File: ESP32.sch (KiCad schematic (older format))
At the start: 28 parts, among them J201 Conn_02x13_Odd_Even, J202 Conn_02x10_Odd_Even, J203 Conn_01x02, U201 ESP32-WROOM-32D

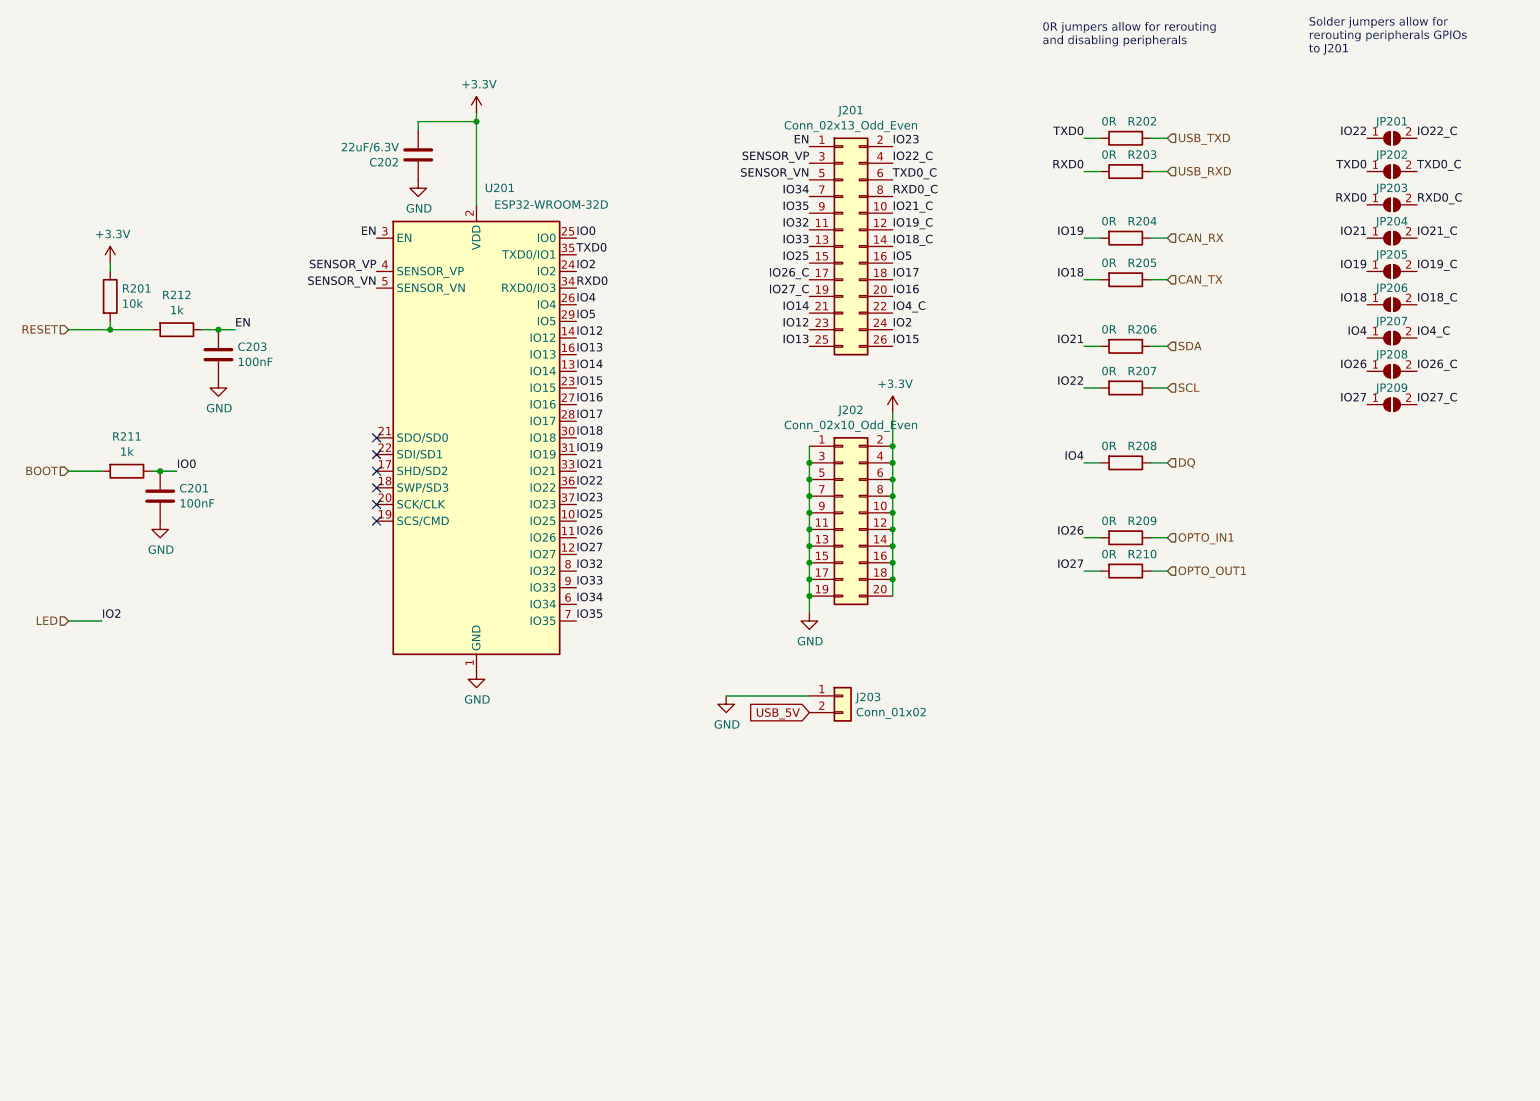
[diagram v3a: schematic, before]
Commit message: Change optocoupler types, improve ground planes and a lot of other smaller fixes
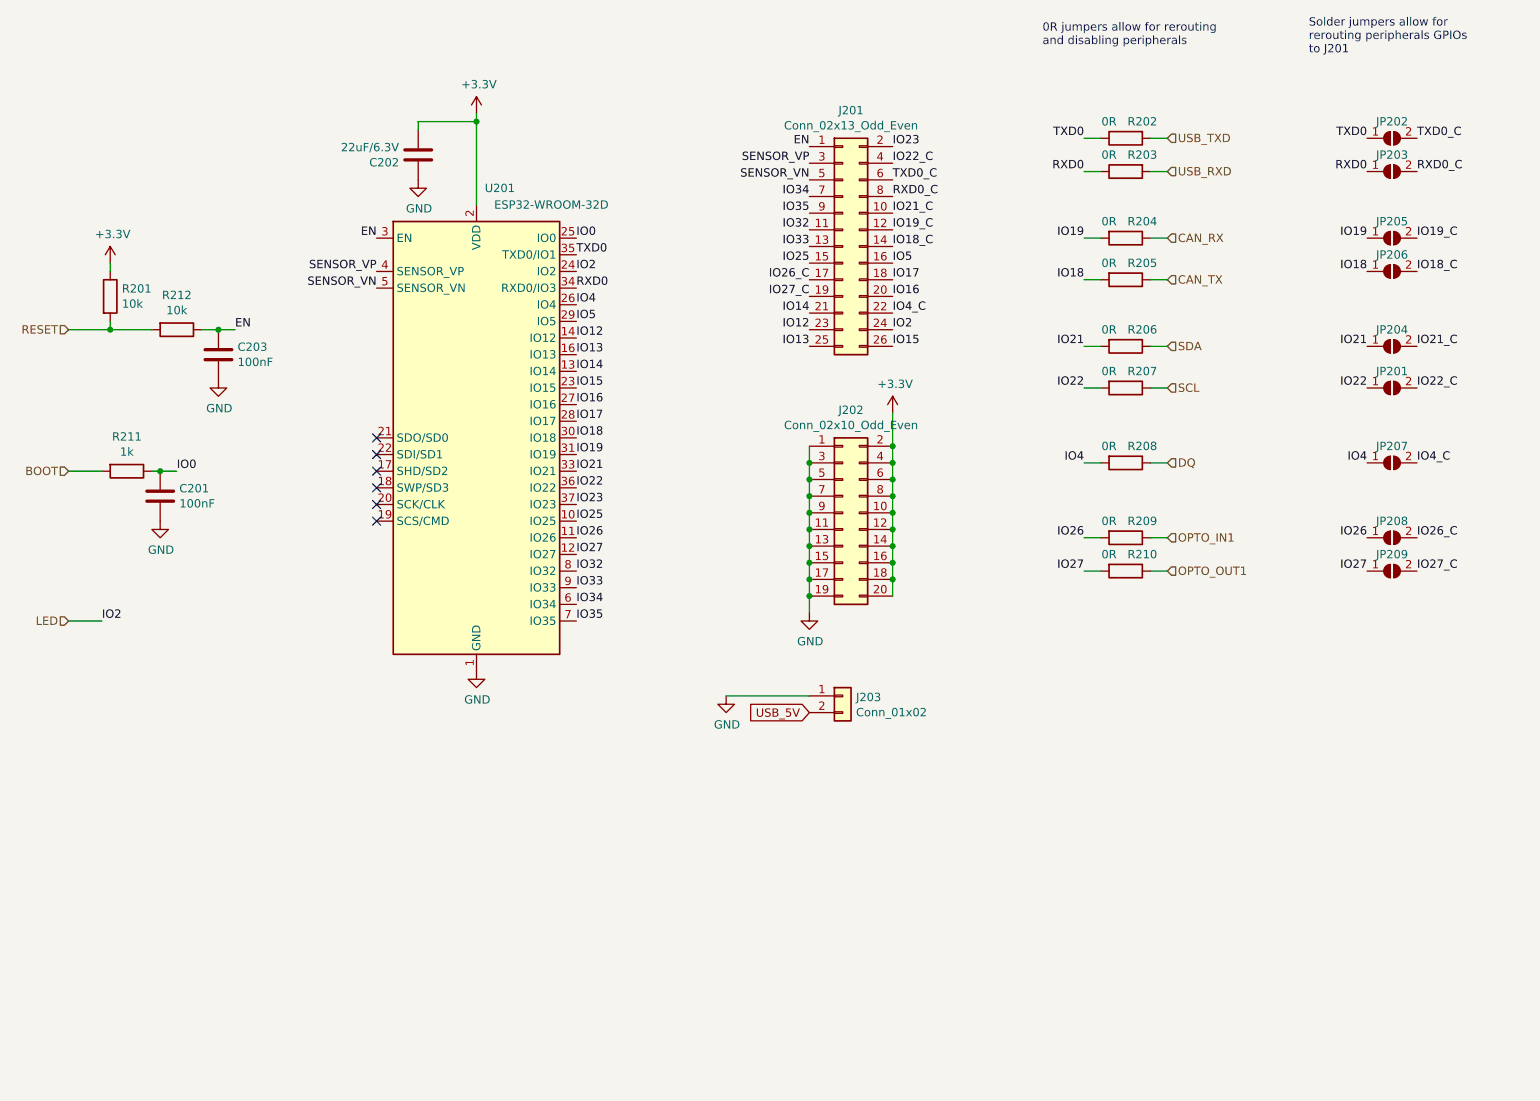
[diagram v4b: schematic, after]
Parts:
- R212: value 1k -> 10k; LCSC C11702 -> C25744
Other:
- moved on the sheet: JP201, JP202, JP203, JP204, JP205, JP206, JP207, JP208, JP209
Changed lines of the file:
@@
 P 1900 2600
 F 0 "R212" V 1693 2600 50  0000 C CNN
-F 1 "1k" V 1784 2600 50  0000 C CNN
+F 1 "10k" V 1784 2600 50  0000 C CNN
 F 2 "Resistor_SMD:R_0402_1005Metric" V 1830 2600 50  0001 C CNN
 F 3 "~" H 1900 2600 50  0001 C CNN
-F 4 "C11702" H 1900 2600 50  0001 C CNN "LCSC"
+F 4 "C25744" H 1900 2600 50  0001 C CNN "LCSC"
 	1    1900 2600
 	0    1    1    0
@@
 	1    0    0    -1
 $EndComp
+Text Label 9350 2950 0    50   ~ 0
+IO22_C
 Text Label 9350 1450 0    50   ~ 0
-IO22_C
+TXD0_C
 Text Label 9350 1650 0    50   ~ 0
-TXD0_C
-Text Label 9350 1850 0    50   ~ 0
 RXD0_C
+Text Label 9350 2700 0    50   ~ 0
+IO21_C
 Text Label 9350 2050 0    50   ~ 0
-IO21_C
+IO19_C
 Text Label 9350 2250 0    50   ~ 0
-IO19_C
-Text Label 9350 2450 0    50   ~ 0
 IO18_C
-Text Label 9350 2650 0    50   ~ 0
+Text Label 9350 3400 0    50   ~ 0
 IO4_C
-Text Label 9350 2850 0    50   ~ 0
+Text Label 9350 3850 0    50   ~ 0
 IO26_C
-Text Label 9350 3050 0    50   ~ 0
+Text Label 9350 4050 0    50   ~ 0
 IO27_C
+Text Label 9050 2950 2    50   ~ 0
+IO22
 Text Label 9050 1450 2    50   ~ 0
-IO22
+TXD0
 Text Label 9050 1650 2    50   ~ 0
-TXD0
-Text Label 9050 1850 2    50   ~ 0
 RXD0
+Text Label 9050 2700 2    50   ~ 0
+IO21
 Text Label 9050 2050 2    50   ~ 0
-IO21
+IO19
 Text Label 9050 2250 2    50   ~ 0
-IO19
-Text Label 9050 2450 2    50   ~ 0
 IO18
-Text Label 9050 2650 2    50   ~ 0
+Text Label 9050 3400 2    50   ~ 0
 IO4
-Text Label 9050 2850 2    50   ~ 0
+Text Label 9050 3850 2    50   ~ 0
 IO26
-Text Label 9050 3050 2    50   ~ 0
+Text Label 9050 4050 2    50   ~ 0
 IO27
 $Comp
 L Jumper:SolderJumper_2_Open JP201
 U 1 1 5FB7A6EE
+P 9200 2950
+F 0 "JP201" H 9200 3050 50  0000 C CNN
+F 1 "SolderJumper_2_Open" H 9200 3064 50  0001 C CNN
+F 2 "SH-ESP32:SolderJumper-2_P1.3mm_Open_TrianglePad_Narrow" H 9200 2950 50  0001 C CNN
+F 3 "~" H 9200 2950 50  0001 C CNN
+	1    9200 2950
+	1    0    0    -1
+$EndComp
+$Comp
+L Jumper:SolderJumper_2_Open JP202
+U 1 1 5FB7C918
 P 9200 1450
-F 0 "JP201" H 9200 1550 50  0000 C CNN
+F 0 "JP202" H 9200 1550 50  0000 C CNN
 F 1 "SolderJumper_2_Open" H 9200 1564 50  0001 C CNN
 F 2 "SH-ESP32:SolderJumper-2_P1.3mm_Open_TrianglePad_Narrow" H 9200 1450 50  0001 C CNN
@@
 $EndComp
 $Comp
-L Jumper:SolderJumper_2_Open JP202
-U 1 1 5FB7C918
+L Jumper:SolderJumper_2_Open JP203
+U 1 1 5FB7CDD7
 P 9200 1650
-F 0 "JP202" H 9200 1750 50  0000 C CNN
+F 0 "JP203" H 9200 1750 50  0000 C CNN
 F 1 "SolderJumper_2_Open" H 9200 1764 50  0001 C CNN
 F 2 "SH-ESP32:SolderJumper-2_P1.3mm_Open_TrianglePad_Narrow" H 9200 1650 50  0001 C CNN
@@
 $EndComp
 $Comp
-L Jumper:SolderJumper_2_Open JP203
-U 1 1 5FB7CDD7
-P 9200 1850
-F 0 "JP203" H 9200 1950 50  0000 C CNN
-F 1 "SolderJumper_2_Open" H 9200 1964 50  0001 C CNN
-F 2 "SH-ESP32:SolderJumper-2_P1.3mm_Open_TrianglePad_Narrow" H 9200 1850 50  0001 C CNN
-F 3 "~" H 9200 1850 50  0001 C CNN
-	1    9200 1850
-	1    0    0    -1
-$EndComp
-$Comp
 L Jumper:SolderJumper_2_Open JP204
 U 1 1 5FB7D1DC
+P 9200 2700
+F 0 "JP204" H 9200 2800 50  0000 C CNN
+F 1 "SolderJumper_2_Open" H 9200 2814 50  0001 C CNN
+F 2 "SH-ESP32:SolderJumper-2_P1.3mm_Open_TrianglePad_Narrow" H 9200 2700 50  0001 C CNN
+F 3 "~" H 9200 2700 50  0001 C CNN
+	1    9200 2700
+	1    0    0    -1
+$EndComp
+$Comp
+L Jumper:SolderJumper_2_Open JP205
+U 1 1 5FB7D48C
 P 9200 2050
-F 0 "JP204" H 9200 2150 50  0000 C CNN
+F 0 "JP205" H 9200 2150 50  0000 C CNN
 F 1 "SolderJumper_2_Open" H 9200 2164 50  0001 C CNN
 F 2 "SH-ESP32:SolderJumper-2_P1.3mm_Open_TrianglePad_Narrow" H 9200 2050 50  0001 C CNN
@@
 $EndComp
 $Comp
-L Jumper:SolderJumper_2_Open JP205
-U 1 1 5FB7D48C
+L Jumper:SolderJumper_2_Open JP206
+U 1 1 5FB7D7F6
 P 9200 2250
-F 0 "JP205" H 9200 2350 50  0000 C CNN
+F 0 "JP206" H 9200 2350 50  0000 C CNN
 F 1 "SolderJumper_2_Open" H 9200 2364 50  0001 C CNN
 F 2 "SH-ESP32:SolderJumper-2_P1.3mm_Open_TrianglePad_Narrow" H 9200 2250 50  0001 C CNN
@@
 $EndComp
 $Comp
-L Jumper:SolderJumper_2_Open JP206
-U 1 1 5FB7D7F6
-P 9200 2450
-F 0 "JP206" H 9200 2550 50  0000 C CNN
-F 1 "SolderJumper_2_Open" H 9200 2564 50  0001 C CNN
-F 2 "SH-ESP32:SolderJumper-2_P1.3mm_Open_TrianglePad_Narrow" H 9200 2450 50  0001 C CNN
-F 3 "~" H 9200 2450 50  0001 C CNN
-	1    9200 2450
-	1    0    0    -1
-$EndComp
-$Comp
 L Jumper:SolderJumper_2_Open JP207
 U 1 1 5FB7DA87
-P 9200 2650
-F 0 "JP207" H 9200 2750 50  0000 C CNN
-F 1 "SolderJumper_2_Open" H 9200 2764 50  0001 C CNN
-F 2 "SH-ESP32:SolderJumper-2_P1.3mm_Open_TrianglePad_Narrow" H 9200 2650 50  0001 C CNN
-F 3 "~" H 9200 2650 50  0001 C CNN
-	1    9200 2650
+P 9200 3400
+F 0 "JP207" H 9200 3500 50  0000 C CNN
+F 1 "SolderJumper_2_Open" H 9200 3514 50  0001 C CNN
+F 2 "SH-ESP32:SolderJumper-2_P1.3mm_Open_TrianglePad_Narrow" H 9200 3400 50  0001 C CNN
+F 3 "~" H 9200 3400 50  0001 C CNN
+	1    9200 3400
 	1    0    0    -1
 $EndComp
@@
 L Jumper:SolderJumper_2_Open JP208
 U 1 1 5FB7E3FF
-P 9200 2850
-F 0 "JP208" H 9200 2950 50  0000 C CNN
-F 1 "SolderJumper_2_Open" H 9200 2964 50  0001 C CNN
-F 2 "SH-ESP32:SolderJumper-2_P1.3mm_Open_TrianglePad_Narrow" H 9200 2850 50  0001 C CNN
-F 3 "~" H 9200 2850 50  0001 C CNN
-	1    9200 2850
+P 9200 3850
+F 0 "JP208" H 9200 3950 50  0000 C CNN
+F 1 "SolderJumper_2_Open" H 9200 3964 50  0001 C CNN
+F 2 "SH-ESP32:SolderJumper-2_P1.3mm_Open_TrianglePad_Narrow" H 9200 3850 50  0001 C CNN
+F 3 "~" H 9200 3850 50  0001 C CNN
+	1    9200 3850
 	1    0    0    -1
 $EndComp
@@
 L Jumper:SolderJumper_2_Open JP209
 U 1 1 5FB7EB87
-P 9200 3050
-F 0 "JP209" H 9200 3150 50  0000 C CNN
-F 1 "SolderJumper_2_Open" H 9200 3164 50  0001 C CNN
-F 2 "SH-ESP32:SolderJumper-2_P1.3mm_Open_TrianglePad_Narrow" H 9200 3050 50  0001 C CNN
-F 3 "~" H 9200 3050 50  0001 C CNN
-	1    9200 3050
-	1    0    0    -1
-$EndComp
+P 9200 4050
+F 0 "JP209" H 9200 4150 50  0000 C CNN
+F 1 "SolderJumper_2_Open" H 9200 4164 50  0001 C CNN
+F 2 "SH-ESP32:SolderJumper-2_P1.3mm_Open_TrianglePad_Narrow" H 9200 4050 50  0001 C CNN
+F 3 "~" H 9200 4050 50  0001 C CNN
+	1    9200 4050
+	1    0    0    -1
+$EndComp

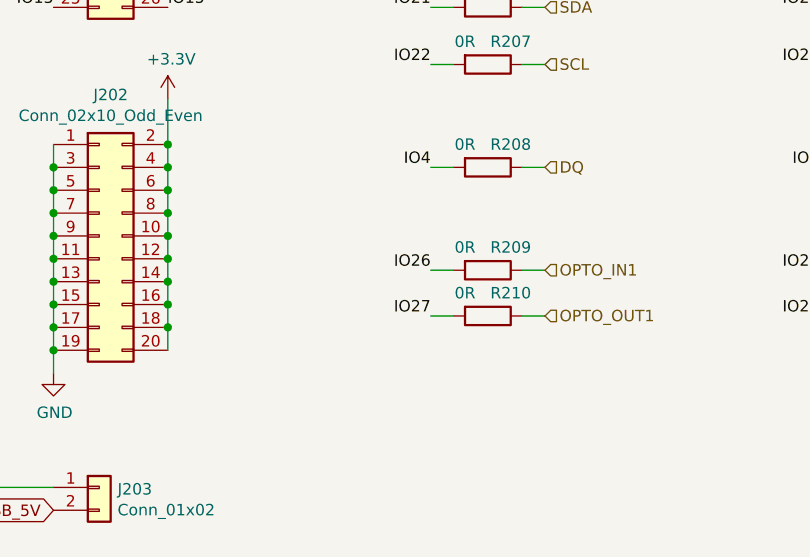
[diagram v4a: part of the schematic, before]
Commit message: Swap optocoupler GPIO pins to connect DAC to output
Not that it makes a lot of difference: the inverting
NPN will behave as a hard switch nevertheless
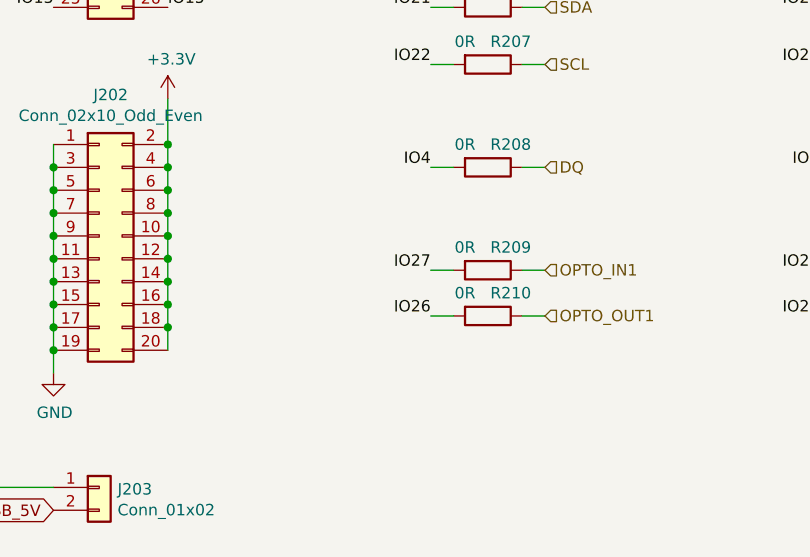
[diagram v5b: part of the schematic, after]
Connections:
- net IO26: now also R210.2; no longer R209.2
- net IO27: now also R209.2; no longer R210.2
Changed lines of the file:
@@
 	0    1    1    0
 $EndComp
-Text Label 7350 3850 2    50   ~ 0
+Text Label 7350 4050 2    50   ~ 0
 IO26
 Wire Wire Line
@@
 Wire Wire Line
 	7850 4050 7750 4050
-Text Label 7350 4050 2    50   ~ 0
+Text Label 7350 3850 2    50   ~ 0
 IO27
 Wire Wire Line

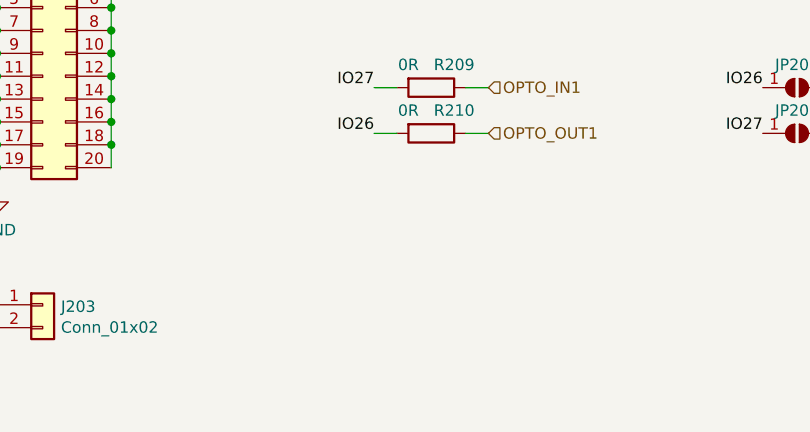
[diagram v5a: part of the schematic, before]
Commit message: Add vertical USB and JTAG Connectors   tp PCB
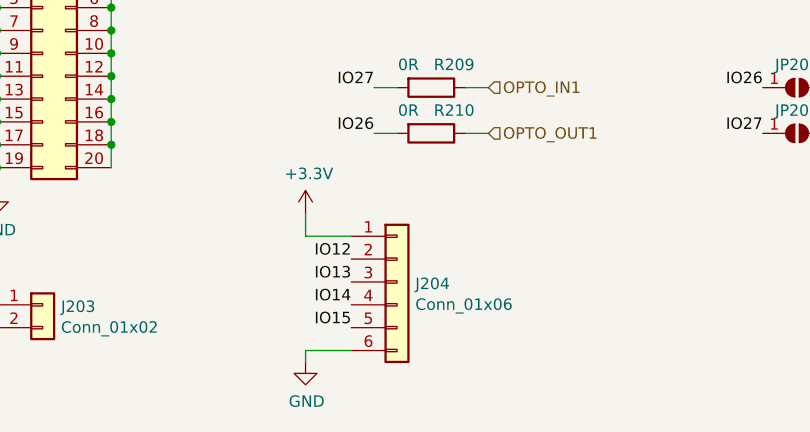
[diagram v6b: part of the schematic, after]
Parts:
- added J204: Conn_01x06, Connector_PinHeader_2.54mm:PinHeader_1x06_P2.54mm_Vertical, symbol Connector_Generic:Conn_01x06
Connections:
- net +3V3: now also J204.1 (Pin_1)
- net GND: now also J204.6 (Pin_6)
- net IO12: now also J204.2 (Pin_2)
- net IO13: now also J204.3 (Pin_3)
- net IO14: now also J204.4 (Pin_4)
- net IO15: now also J204.5 (Pin_5)
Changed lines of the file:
@@
 Text Notes 8700 950  0    50   ~ 0
 Solder jumpers allow for \nrerouting peripherals GPIOs\nto J201
+$Comp
+L Connector_Generic:Conn_01x06 J204
+U 1 1 5FAECE9F
+P 7450 4700
+F 0 "J204" H 7530 4692 50  0000 L CNN
+F 1 "Conn_01x06" H 7530 4601 50  0000 L CNN
+F 2 "Connector_PinHeader_2.54mm:PinHeader_1x06_P2.54mm_Vertical" H 7450 4700 50  0001 C CNN
+F 3 "~" H 7450 4700 50  0001 C CNN
+	1    7450 4700
+	1    0    0    -1
+$EndComp
+$Comp
+L power:GND #PWR0104
+U 1 1 5FAEFBAB
+P 7050 5050
+F 0 "#PWR0104" H 7050 4800 50  0001 C CNN
+F 1 "GND" H 7055 4877 50  0000 C CNN
+F 2 "" H 7050 5050 50  0001 C CNN
+F 3 "" H 7050 5050 50  0001 C CNN
+	1    7050 5050
+	1    0    0    -1
+$EndComp
+Wire Wire Line
+	7250 5000 7050 5000
+Wire Wire Line
+	7050 5000 7050 5050
+$Comp
+L power:+3.3V #PWR?
+U 1 1 5FAF2B1F
+P 7050 4400
+AR Path="/5FAF2B1F" Ref="#PWR?"  Part="1"
+AR Path="/5FC3847D/5FAF2B1F" Ref="#PWR0105"  Part="1"
+F 0 "#PWR0105" H 7050 4250 50  0001 C CNN
+F 1 "+3.3V" H 7065 4573 50  0000 C CNN
+F 2 "" H 7050 4400 50  0001 C CNN
+F 3 "" H 7050 4400 50  0001 C CNN
+	1    7050 4400
+	1    0    0    -1
+$EndComp
+Wire Wire Line
+	7250 4500 7050 4500
+Wire Wire Line
+	7050 4500 7050 4400
+Text Label 7250 4600 2    50   ~ 0
+IO12
+Text Label 7250 4700 2    50   ~ 0
+IO13
+Text Label 7250 4800 2    50   ~ 0
+IO14
+Text Label 7250 4900 2    50   ~ 0
+IO15
 $EndSCHEMATC
